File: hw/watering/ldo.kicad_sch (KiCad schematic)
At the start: 3 parts, among them U7 NCP163AFCT330T2G

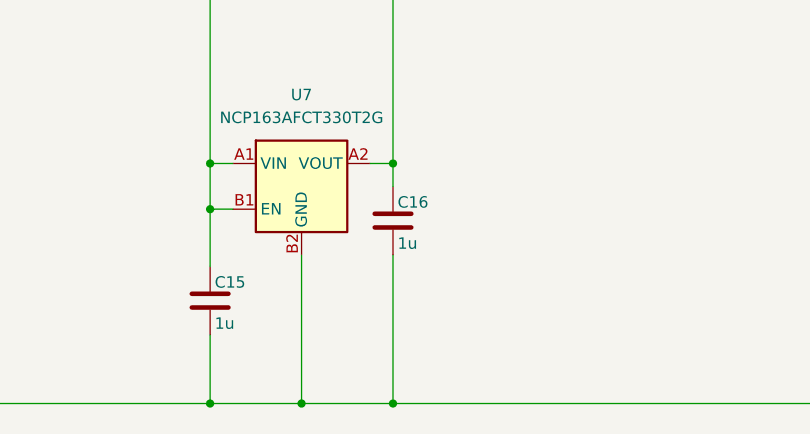
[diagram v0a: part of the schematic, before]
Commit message: connections completet. started placing and routing
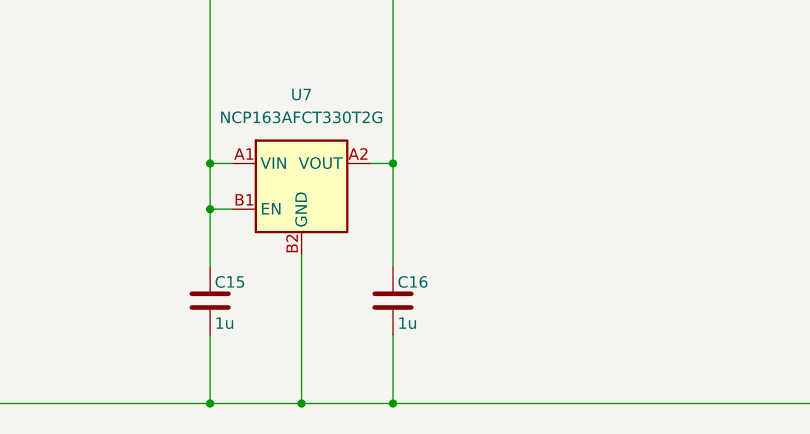
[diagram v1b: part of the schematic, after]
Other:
- moved on the sheet: C16
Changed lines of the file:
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@@
+	)
+	(junction
+		(at 121.92 20.32)
+		(diameter 0)
+		(color 0 0 0 0)
 	)
 	(junction
@@
 	)
 	(junction
-		(at 121.92 20.32)
-		(diameter 0)
-		(color 0 0 0 0)
-	)
-	(junction
 		(at 142.24 22.86)
 		(diameter 0)
@@
 	)
 	(junction
+		(at 142.24 162.56)
+		(diameter 0)
+		(color 0 0 0 0)
+	)
+	(junction
 		(at 121.92 135.89)
 		(diameter 0)
@@
 	)
 	(junction
-		(at 142.24 162.56)
-		(diameter 0)
-		(color 0 0 0 0)
-	)
-	(junction
 		(at 121.92 140.97)
 		(diameter 0)
@@
 	(wire
 		(pts
-			(xy 142.24 138.43) (xy 142.24 135.89)
-		)
-		(stroke
-			(width 0)
-			(type default)
-		)
-	)
-	(wire
-		(pts
-			(xy 142.24 146.05) (xy 142.24 162.56)
+			(xy 142.24 147.32) (xy 142.24 135.89)
+		)
+		(stroke
+			(width 0)
+			(type default)
+		)
+	)
+	(wire
+		(pts
+			(xy 142.24 154.94) (xy 142.24 162.56)
 		)
 		(stroke
@@
 	(symbol
 		(lib_id "Device:C")
-		(at 142.24 142.24 0)
+		(at 142.24 151.13 0)
 		(unit 1)
 		(body_style 1)
@@
 		(dnp no)
 		(property "Reference" "C16"
-			(at 142.748 140.208 0)
+			(at 142.748 149.098 0)
 			(show_name no)
 			(do_not_autoplace no)
@@
 		)
 		(property "Value" "1u"
-			(at 142.748 144.78 0)
+			(at 142.748 153.67 0)
 			(show_name no)
 			(do_not_autoplace no)
@@
 		)
 		(property "Footprint" "Capacitor_SMD:C_0603_1608Metric"
-			(at 143.2052 146.05 0)
+			(at 143.2052 154.94 0)
 			(hide yes)
 			(show_name no)
@@
 		)
 		(property "Datasheet" "https://jlc-prod-smt.oss-eu-central-1.aliyuncs.com/smtDataManualFile/8556213788455567360-C15849.pdf?response-content-disposition=attachment%3B%20filename%3DC15849.pdf%3B%20filename%2A%3DUTF-8%27%27C15849.pdf&x-oss-date=20260604T201738Z&x-oss-expires=1800&x-oss-security-token=CAISgAN1q6Ft5B2yfSjIr5rnDe%2F5h6h02fGfW1HcsFYmaelfp6rpszz2IHhMdHJsAOodtv0%2FmmhT6PkclqRLcbhpcmfjV%2BZHzLB8qeACnUZA4J7b16cNrbH4M4H6aXeirtuwDsz9SNTCALjPD3nPii50x5bjaDymRCbLGJaViJlhHLN1Ow6jdmhpCctxLAlvo9NgFxm3D%2Fu2NQPwiWf9FVdhvhEG6Vly8qOi2MaRmFy8yFTx0b0SvJ%2BjYMrmPctoN9JnSdC5mfdzau3a1TJ84gRD0a5wkaVA1zbDs5bfISEIuUzebreLqY03dV4mOvdqIcMe8qigz88fk%2FfIioH6xyxKOexoSCnFTOiiupCcQLPyao9jLu6iayqViY7QaIOTqQohZmkAMwVOasAsI3Ngh4zF97Qt0cVNkXO9gWfLI8DtuMleWhqD30JB3tHD0eS19jklBdzSlusJRAJJUVBflCeKEaRNSAd3WGhEfM2%2BBt4QT30w5N2u00S8OSMIc%2BkdiqKWD5sagAFWQNkecW6D1E4coUzPadT7SCc3f42V3X5rSfMFH84ElX%2BTmNGNYscgqDx0xyaTJyyrM%2BFQW4w%2FhWX4qrYQWwgwoGw%2BQzNTMlILHbcsYIbLhGAndRWnhNlBy%2F%2FsrfRbXWVyCjftSb4xwrnr%2BixQsq7hkcXqmYOc23lG%2B0BooZpCuSAA&x-oss-signature-version=OSS4-HMAC-SHA256&x-oss-credential=STS.NYRFUMjwUn3tYwmTVsefsHoBQ%2F20260604%2Feu-central-1%2Foss%2Faliyun_v4_request&x-oss-signature=f7f3fdbb1b5574cda7c663cf4e84bef841ee38f93673a2b4cff19ca4130e6e09"
-			(at 142.24 142.24 0)
+			(at 142.24 151.13 0)
 			(hide yes)
 			(show_name no)
@@
 		)
 		(property "Description" "C15849"
-			(at 142.24 142.24 0)
-			(hide yes)
-			(show_name no)
+			(at 142.24 151.13 0)
+			(hide yes)
+			(show_name no)
